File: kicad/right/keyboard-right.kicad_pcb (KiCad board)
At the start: 2 copper layers, 87 parts, among them J1 Conn_01x04_Pin, J2 AudioJack4, J3 Conn_01x04_Pin, J4 Conn_01x04_Pin, J5 Conn_01x02_Pin, SW1 SW_Push, SW10 SW_Push, SW11 SW_Push, SW12 SW_Push, SW13 SW_Push, SW14 SW_Push, SW15 SW_Push, SW16 SW_Push, SW17 SW_Push, SW18 SW_Push, SW19 SW_Push, SW2 SW_Push, SW20 SW_Push, SW21 SW_Push, SW22 SW_Push, SW23 SW_Push, SW24 SW_Push, SW25 SW_Push, SW26 SW_Push, SW27 SW_Push, SW28 SW_Push, SW29 SW_Push, SW3 SW_Push, SW30 SW_Push, SW31 SW_Push, SW32 SW_Push, SW33 SW_Push, SW34 SW_Push, SW35 SW_Push, SW36 SW_Push, SW4 SW_Push, SW5 SW_Push, SW6 SW_Push, SW7 SW_Push, SW8 SW_Push, SW9 SW_Push, U1 AVR32DA32x-xPT

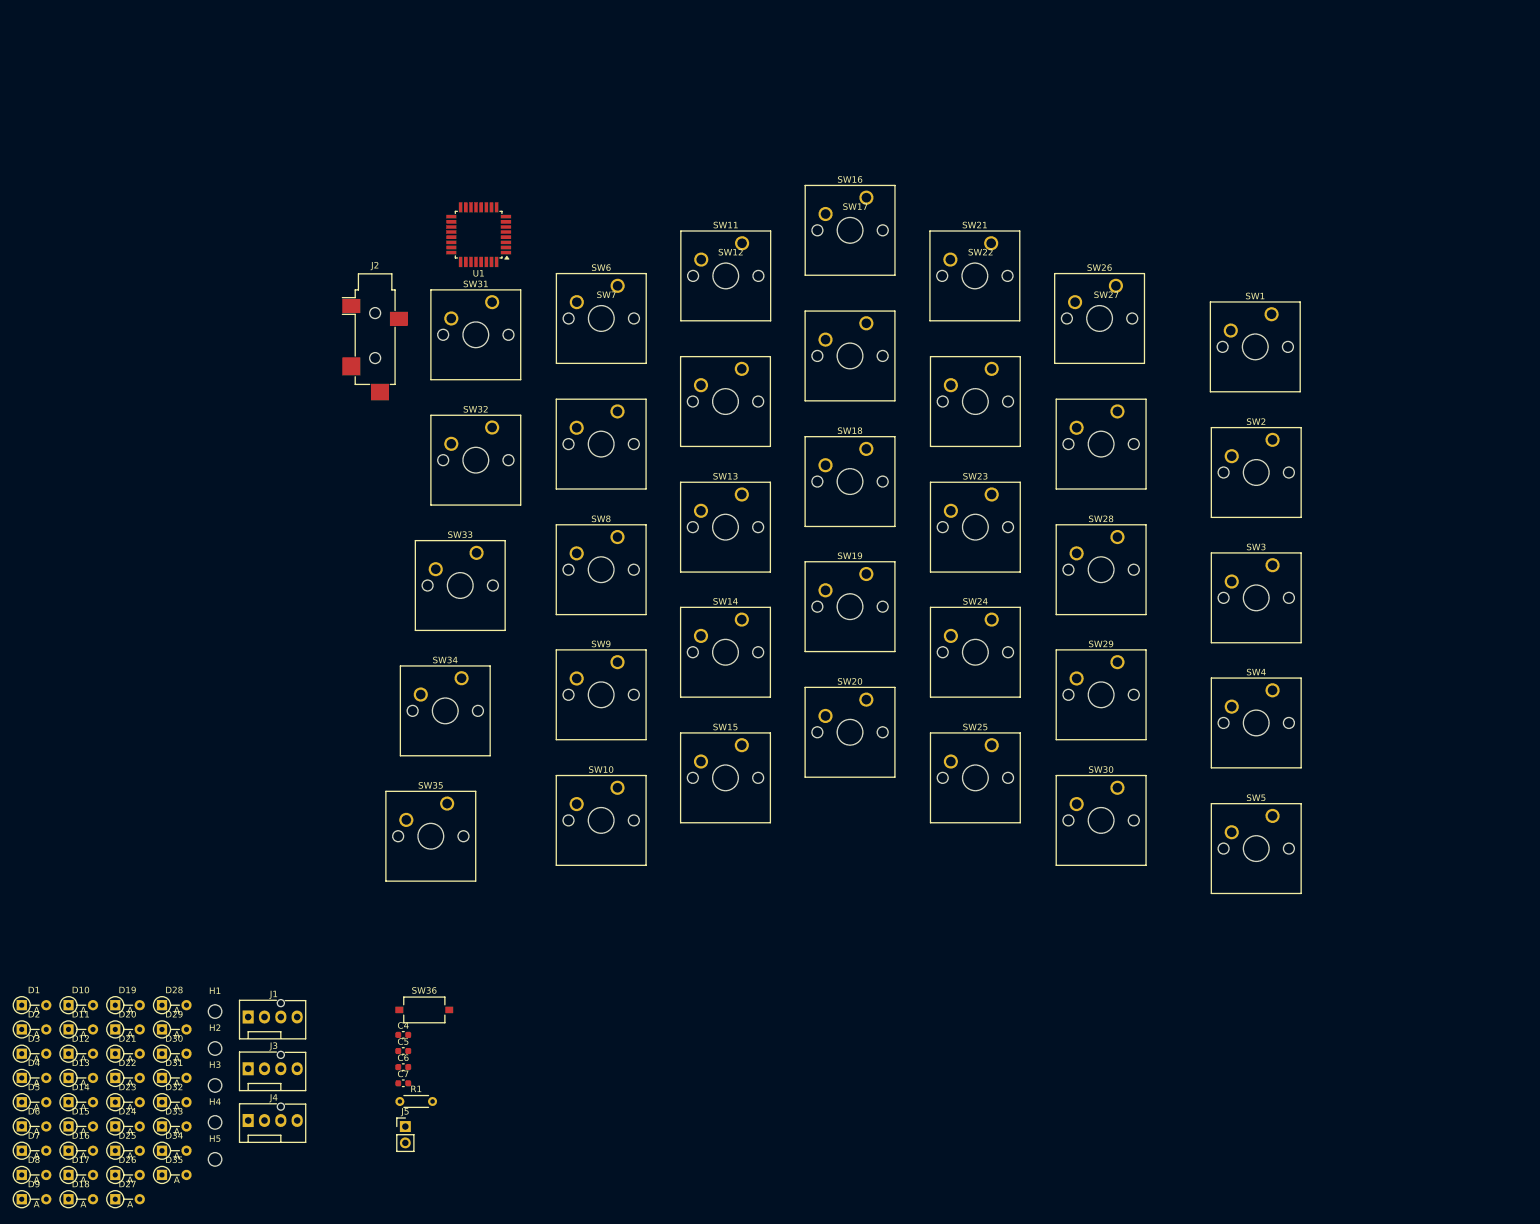
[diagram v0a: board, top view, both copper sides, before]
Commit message: finished up right side pcb
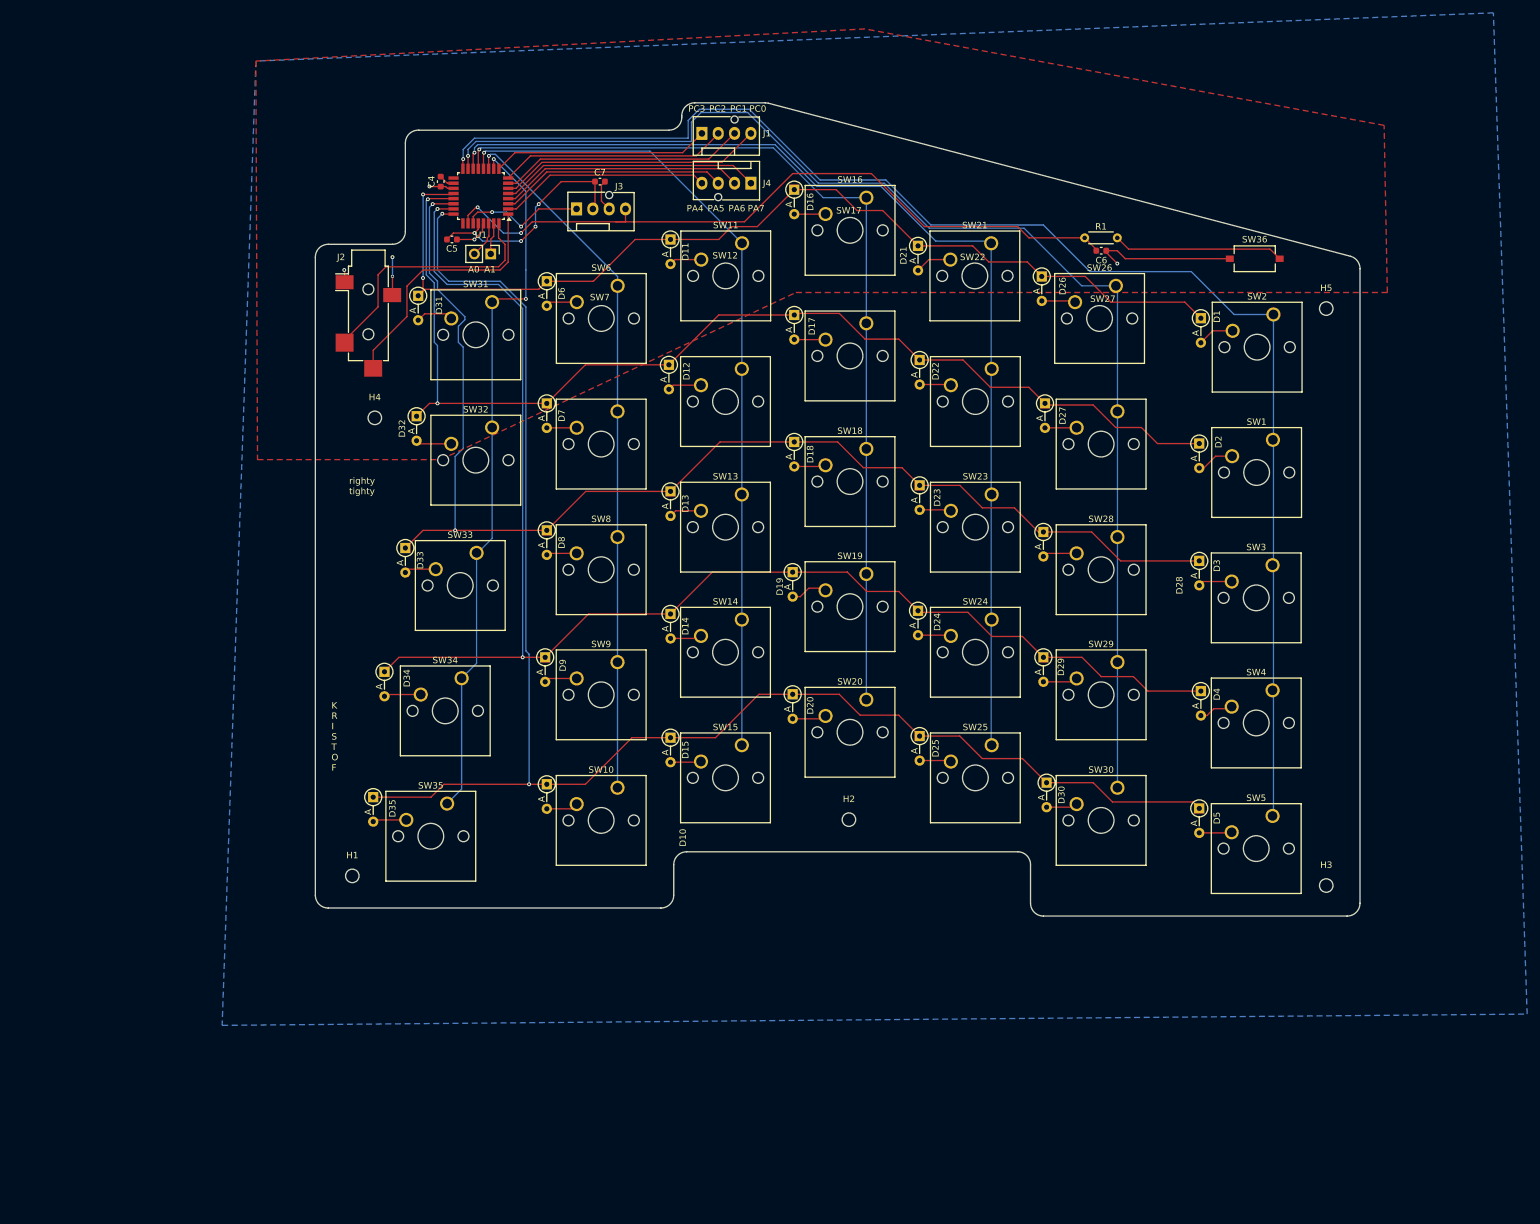
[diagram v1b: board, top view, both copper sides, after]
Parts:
- moved H5 217.7 mm to (223.2, 49.2)
- moved D1 212.3 mm to (203.8, 50.8), turned to -90 degrees
- moved D2 204.6 mm to (203.5, 70.2), turned to -90 degrees
- moved D26 200.8 mm to (179.0, 44.2), turned to -90 degrees
- moved D3 198.6 mm to (203.5, 88.5), turned to -90 degrees
- moved D4 193.0 mm to (203.8, 108.8), turned to -90 degrees
- moved D27 190.4 mm to (179.5, 64.0), turned to -90 degrees
- moved D5 188.8 mm to (203.5, 127.0), turned to -90 degrees
- moved D16 187.3 mm to (140.5, 30.8), turned to -90 degrees
- moved D21 177.2 mm to (159.8, 39.5), turned to -90 degrees
- moved H3 175.6 mm to (223.2, 139.0)
- moved D17 175.0 mm to (140.5, 50.3), turned to -90 degrees
- moved R1 174.6 mm to (190.8, 38.2), turned to 180 degrees
- moved SW36 174.2 mm to (212.1, 41.5)
- moved D22 167.7 mm to (160.0, 57.3), turned to -90 degrees
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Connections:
- SW1 pad 1: col1 -> col7
- SW2 pad 1: col1 -> col7
- SW3 pad 1: col1 -> col7
- SW31 pad 1: col7 -> col1
- SW32 pad 1: col7 -> col1
- SW33 pad 1: col7 -> col1
- SW34 pad 1: col7 -> col1
- SW35 pad 1: col7 -> col1
- SW4 pad 1: col1 -> col7
- SW5 pad 1: col1 -> col7
- U1 pad 29: unconnected-(U1-GND-Pad29) -> GND
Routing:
- net row5: track 0.00 -> 243.9 mm, vias 0 -> 2
- net col7: track 0.00 -> 224.5 mm, vias 0 -> 1
- net row4: track 0.00 -> 223.9 mm, vias 0 -> 2
- net col6: track 0.00 -> 197.3 mm, vias 0 -> 1
- net row3: track 0.00 -> 195.7 mm, vias 0 -> 2
- net row2: track 0.00 -> 173.4 mm, vias 0 -> 2
- net col5: track 0.00 -> 168.4 mm, vias 0 -> 1
- net row1: track 0.00 -> 157.7 mm, vias 0 -> 2
- net col4: track 0.00 -> 144.7 mm, vias 0 -> 1
- net col3: track 0.00 -> 126.8 mm, vias 0 -> 1
- net Net-(J3-Pin_4): track 0.00 -> 113.6 mm, vias 0 -> 2
- net col1: track 0.00 -> 111.8 mm, vias 0 -> 2
- net col2: track 0.00 -> 109.6 mm, vias 0 -> 1
- net VDD: track 0.00 -> 44.2 mm, vias 0 -> 6
- net Net-(J1-Pin_4): track 0.00 -> 41.3 mm
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- added copper zone on B.Cu, net GND
- added copper zone on F.Cu, net VDD
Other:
- board outline added: 162.5 x 126.5 mm
- board text added: "A0"
- board text added: "A1"
- board text added: "K R I S T O F"
- board text added: "PA4"
- board text added: "PA5"
- board text added: "PA6"
- board text added: "PA7"
- board text added: "PC0"
- board text added: "PC1"
- board text added: "PC2"
- board text added: "PC3"
- board text added: "righty tighty"
